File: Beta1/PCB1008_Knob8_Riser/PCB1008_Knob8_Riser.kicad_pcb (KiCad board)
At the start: 2 copper layers, 160 x 75.5 mm, 56 parts, among them J1 Axoloti_40Pin, J2 FPC_20POS, U1 MCP3008T-I/SL, U10 OLED_128x32_I2C, U2 MCP3008T-I/SL, U20 OLED_128x32_I2C, U3 I2C_1x4MUX_TCA9546A, U30 OLED_128x32_I2C, U40 OLED_128x32_I2C

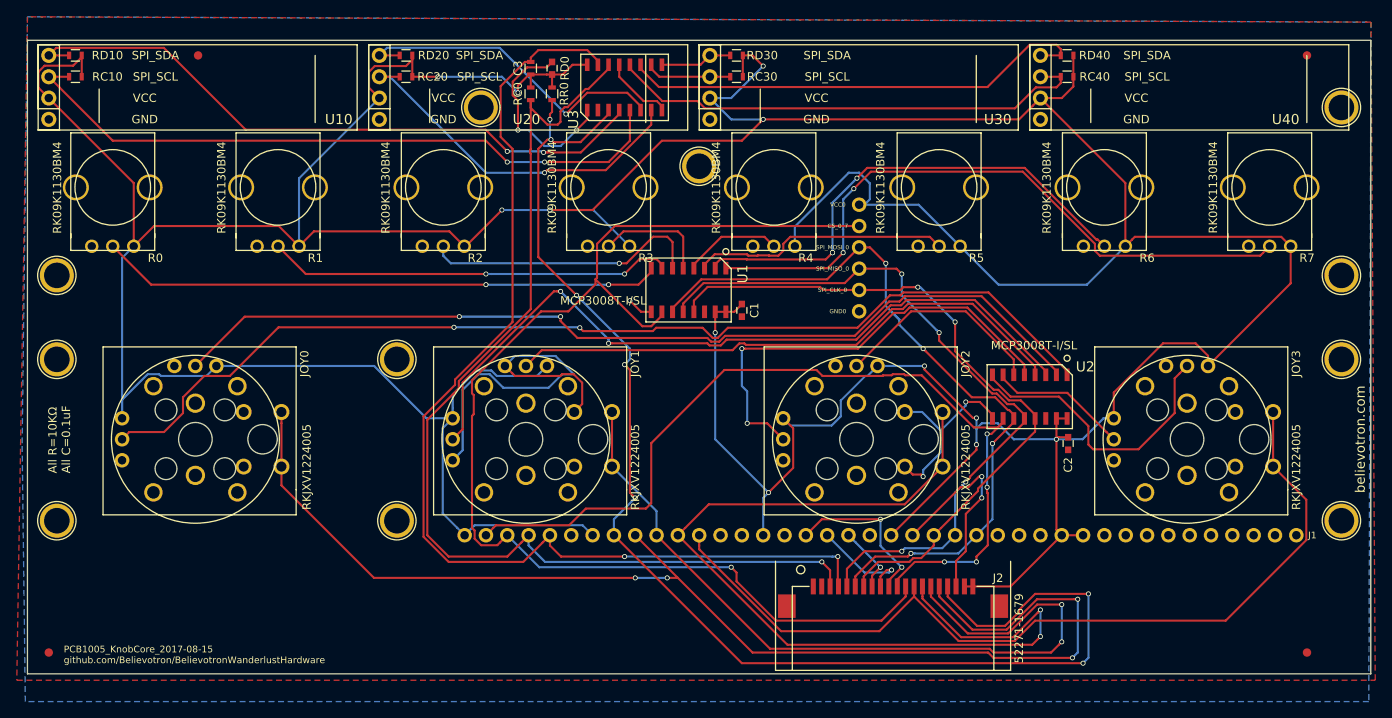
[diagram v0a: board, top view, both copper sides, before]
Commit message: Removed Joysticks / OLED. Read for fab
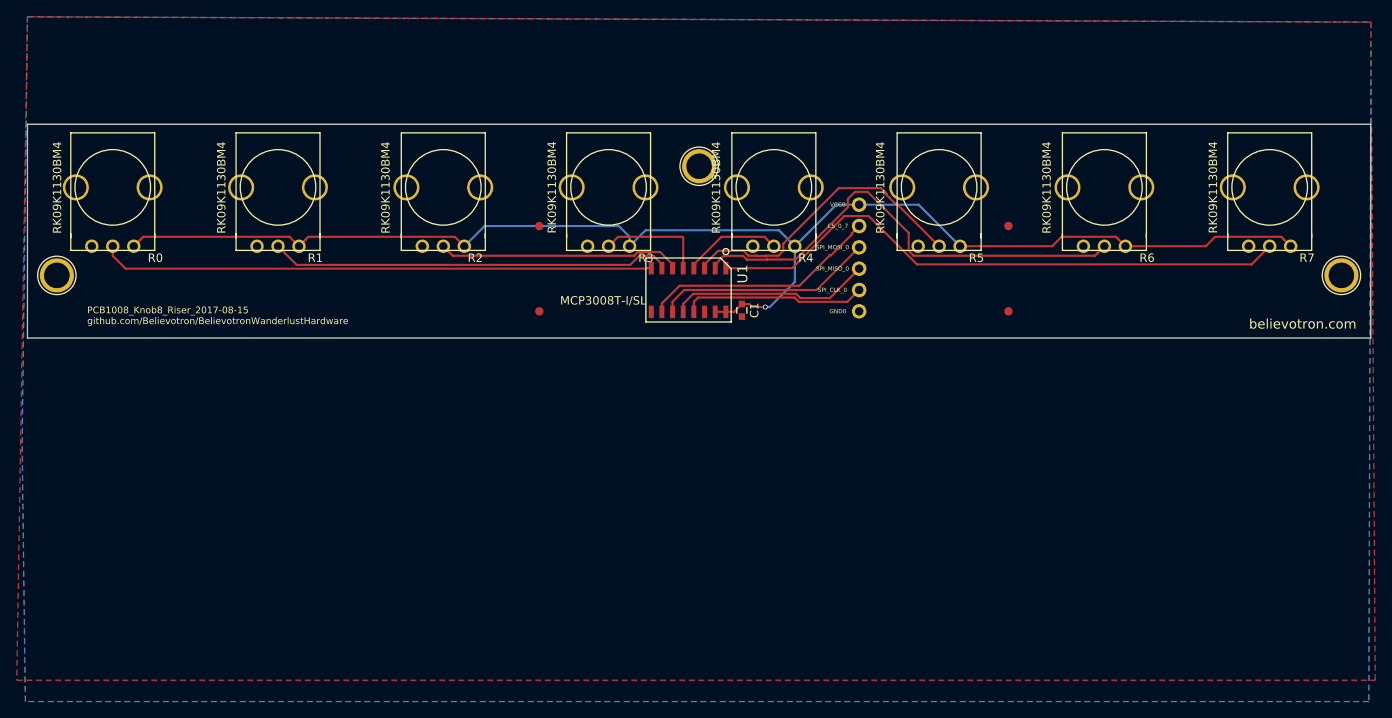
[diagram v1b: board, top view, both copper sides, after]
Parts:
- removed C2, C3: 0.1u, Capacitors_SMD:C_0603
- removed J1: Axoloti_40Pin, Liberry:Axoloti-40x1_slim
- removed J2: FPC_20POS, Liberry:FFC_1MM_20POS_MOLEX_52271-2079
- removed JOY0, JOY1, JOY2, JOY3: XYJOY_Alps, Liberry:JOY_ALPS_RKJXV1224005
- removed RC0, RC10, RC20, RC30, RC40, RD0, RD10, RD20, RD30, RD40, RR0: 10K, Resistors_SMD:R_0603
- removed the REF** at (156.5, -22.2)
- removed the REF** at (156.5, -52.2)
- removed the REF** at (54.0, -52.2)
- removed the REF** at (44.0, -22.2)
- removed the REF** at (156.5, -3.00)
- removed the REF** at (44.0, -3.00)
- removed the REF** at (3.50, -3.00)
- removed the REF** at (3.50, -22.2)
- removed U10, U20, U30, U40: OLED_128x32_I2C, Liberry:OLED_128x32
- removed U2: MCP3008T-I/SL, Liberry:SOIC-16
- removed U3: I2C_1x4MUX_TCA9546A, Liberry:SOIC-16_1.27x5.4
- moved REF** 71.2 mm to (61.0, -27.9)
- moved REF** 54.0 mm to (116.8, -27.9)
- moved REF** 45.4 mm to (61.0, -38.1)
- moved REF** 41.0 mm to (116.8, -38.1)
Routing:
- net +3V3: track 647.5 -> 165.4 mm, vias 12 -> 1
- net /!OLED_RESET: track 159.9 -> 0.00 mm, vias 7 -> 0
- net /JOY_0_SW: track 146.7 -> 0.00 mm, vias 4 -> 0
- net /I2C_SDA: track 130.6 -> 0.00 mm, vias 2 -> 0
- net /JOY_0_0: track 126.6 -> 0.00 mm, vias 2 -> 0
- net /I2C_SCL: track 126.4 -> 0.00 mm, vias 1 -> 0
- net /CS_0_7: track 146.2 -> 28.4 mm, vias 1 -> 0
- net /JOY_0_1: track 112.9 -> 0.00 mm, vias 2 -> 0
- net /JOY_2_SW: track 112.3 -> 0.00 mm, vias 2 -> 0
- net /CS_8_15: track 107.1 -> 0.00 mm, vias 4 -> 0
- net GND: track 105.7 -> 0.00 mm, vias 5 -> 0
- net /JOY_3_SW: track 105.0 -> 0.00 mm
- net /JOY_1_SW: track 95.9 -> 0.00 mm, vias 2 -> 0
- net /JOY_1_0: track 90.3 -> 0.00 mm, vias 2 -> 0
- net /I2C_SCL0: track 80.5 -> 0.00 mm, vias 2 -> 0
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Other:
- board size 160 x 75.5 mm -> 160 x 25.5 mm
- board text added: "PCB1008_Knob8_Riser_2017-08-15 github.com/Believotron/BelievotronWanderlustHardware"
- board text removed: "All R=10KΩ All C=0.1uF"
- board text removed: "PCB1005_KnobCore_2017-08-15 github.com/Believotron/BelievotronWanderlustHardware"
- board text removed: "RKJXV1224005"
